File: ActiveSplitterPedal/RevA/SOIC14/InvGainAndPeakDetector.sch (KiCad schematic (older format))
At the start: 16 parts, among them U1 TL074, U5 TPS60400

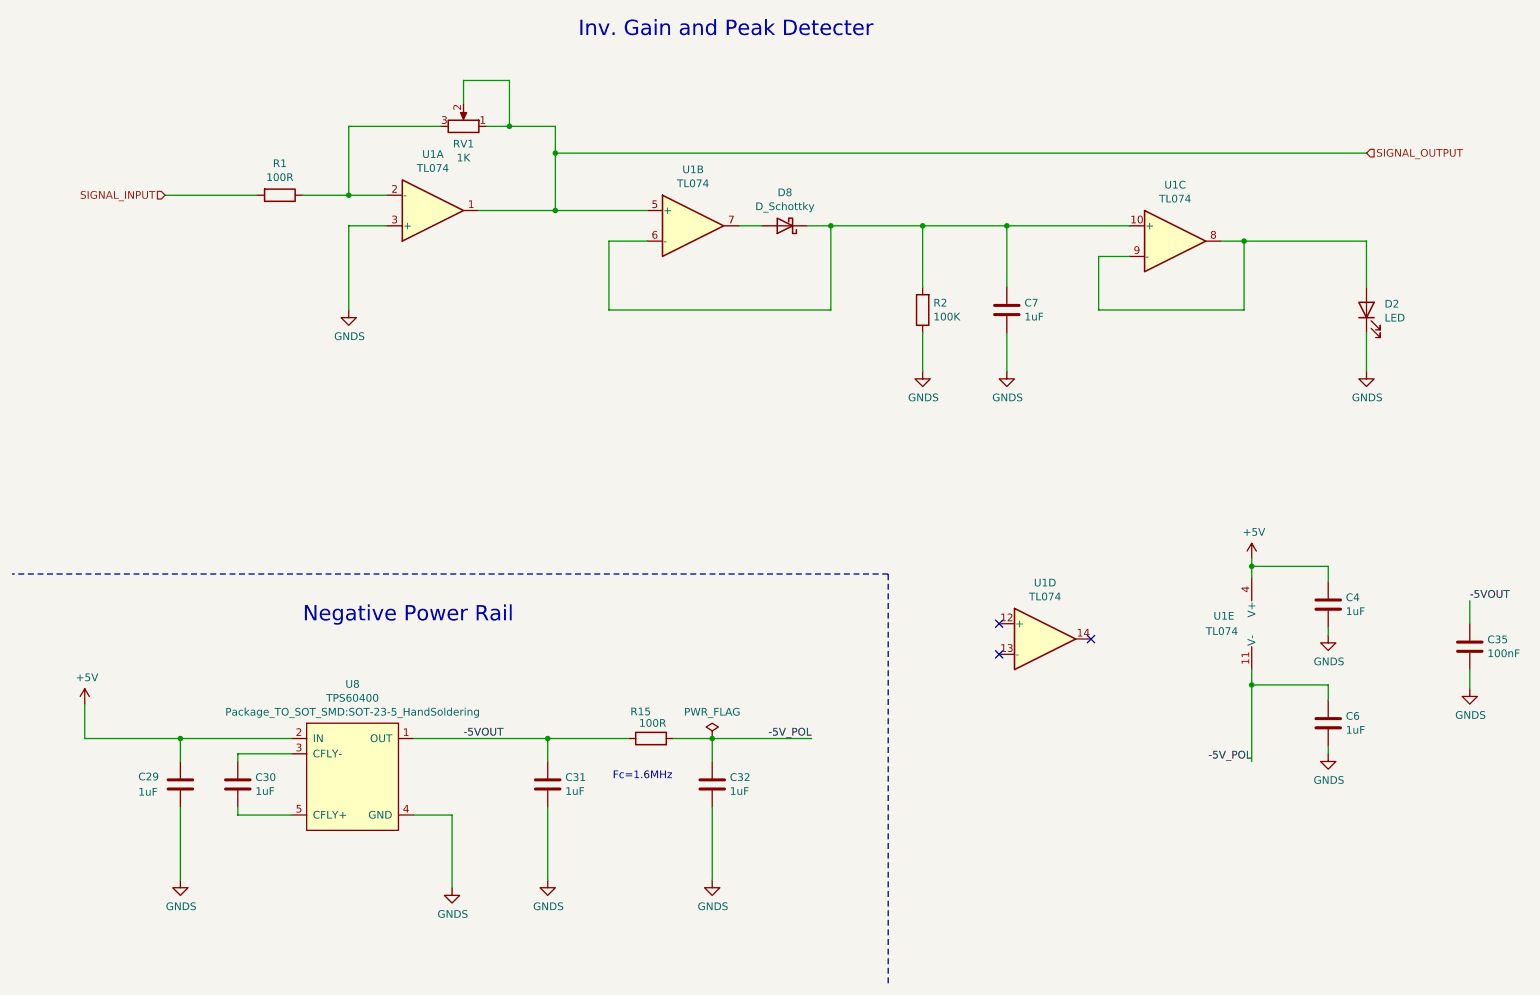
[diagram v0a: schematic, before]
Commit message: updated hw
- Updated RevA charge pump RC post  filter component values for Fc=72KHz
- Updated RevA for gain opamp components
- Branched off RevB to improve design to use internal gain for peak detector
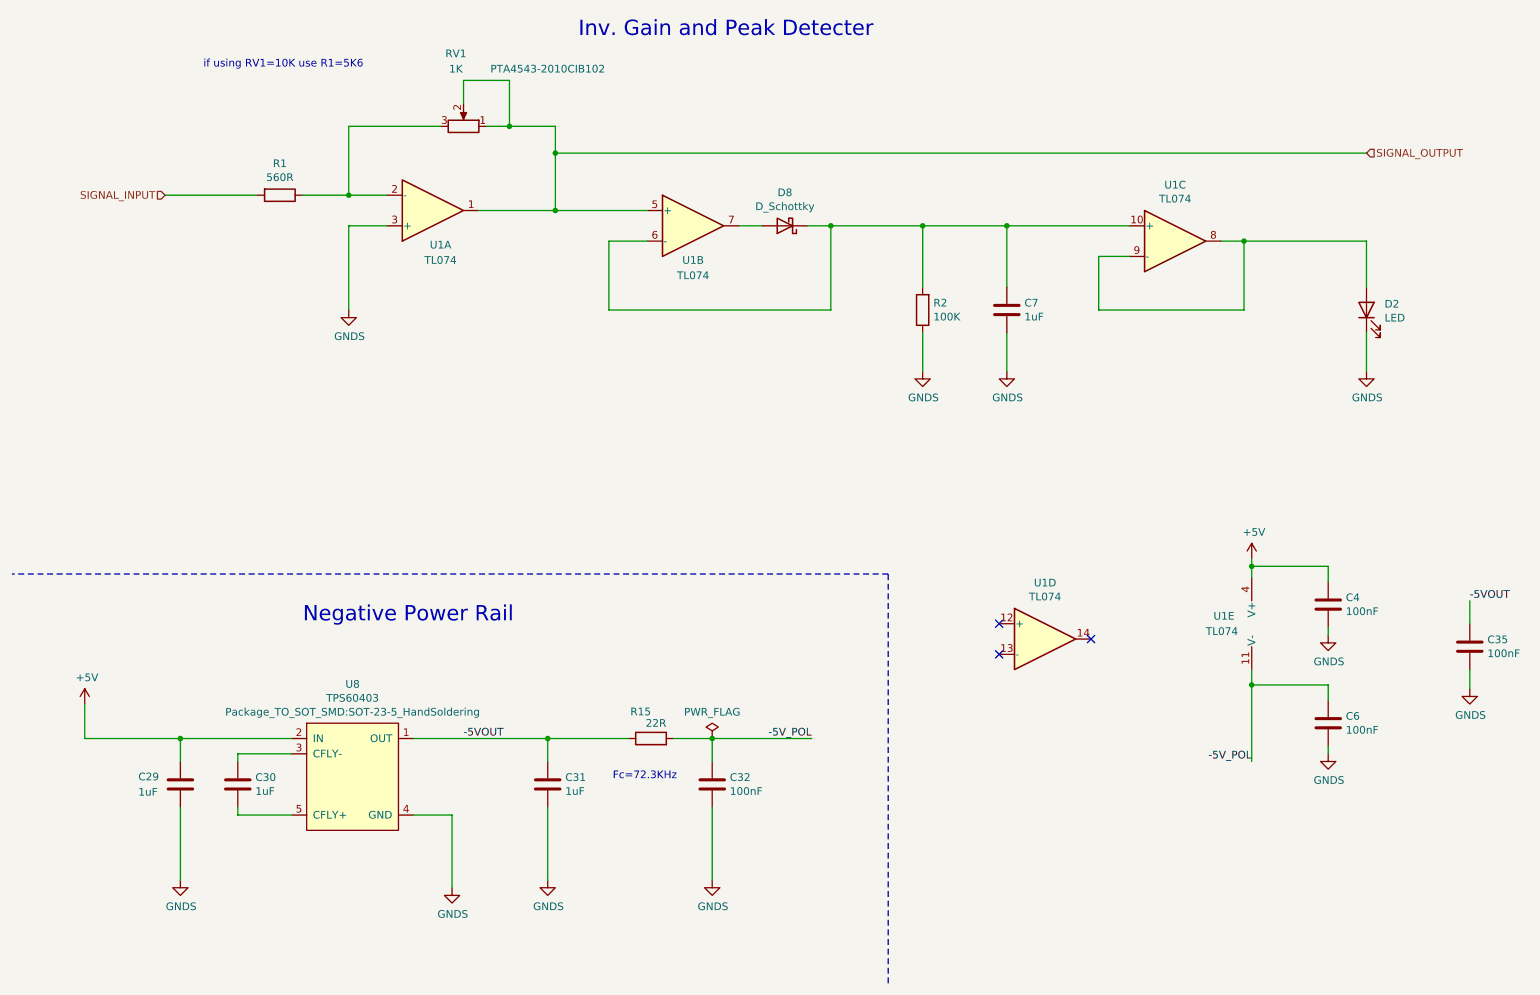
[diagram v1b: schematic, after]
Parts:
- C11, C4, C6: value 1uF -> 100nF
- R1: value 100R -> 560R
- R8: value 100R -> 22R
- RV1: Part No. (none) -> PTA4543-2010CIB102
- U5: value TPS60400 -> TPS60403
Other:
- note added: "Fc=72.3KHz"
- note added: "if using RV1=10K use R1=5K6"
- note removed: "Fc=1.6MHz"
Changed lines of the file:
@@
 $Descr A4 11693 8268
 encoding utf-8
-Sheet 6 6
+Sheet 3 6
 Title ""
 Date ""
@@
 AR Path="/5F515E89/5F3F57C8" Ref="U3"  Part="1"
 AR Path="/5F519B24/5F3F57C8" Ref="U4"  Part="1"
-F 0 "U1" H 3500 2158 50  0000 C CNN
-F 1 "TL074" H 3500 2249 50  0000 C CNN
+F 0 "U1" H 3550 2750 50  0000 C CNN
+F 1 "TL074" H 3550 2850 50  0000 C CNN
 F 2 "Package_SO:SOIC-14_3.9x8.7mm_P1.27mm" H 3450 2625 50  0001 C CNN
 F 3 "http://www.ti.com/lit/ds/symlink/tl071.pdf" H 3550 2725 50  0001 C CNN
@@
 AR Path="/5F515E89/5F3F63C2" Ref="U3"  Part="2"
 AR Path="/5F519B24/5F3F63C2" Ref="U4"  Part="2"
-F 0 "U1" H 5200 2992 50  0000 C CNN
-F 1 "TL074" H 5200 2901 50  0000 C CNN
+F 0 "U1" H 5200 2400 50  0000 C CNN
+F 1 "TL074" H 5200 2300 50  0000 C CNN
 F 2 "Package_SO:SOIC-14_3.9x8.7mm_P1.27mm" H 5150 2725 50  0001 C CNN
 F 3 "http://www.ti.com/lit/ds/symlink/tl071.pdf" H 5250 2825 50  0001 C CNN
@@
 AR Path="/5F519B24/5F415E0A" Ref="R11"  Part="1"
 F 0 "R1" V 2293 2425 50  0000 C CNN
-F 1 "100R" V 2384 2425 50  0000 C CNN
+F 1 "560R" V 2384 2425 50  0000 C CNN
 F 2 "Resistor_SMD:R_0805_2012Metric_Pad1.15x1.40mm_HandSolder" V 2430 2425 50  0001 C CNN
 F 3 "~" H 2500 2425 50  0001 C CNN
@@
 AR Path="/5F515E89/5F4179D2" Ref="RV3"  Part="1"
 AR Path="/5F519B24/5F4179D2" Ref="RV4"  Part="1"
-F 0 "RV1" V 3585 1975 50  0000 C CNN
-F 1 "1K" V 3494 1975 50  0000 C CNN
+F 0 "RV1" V 4175 1925 50  0000 C CNN
+F 1 "1K" V 4075 1925 50  0000 C CNN
 F 2 "Bourn_PTA_Slider:Slider_PTA4543_60MM" H 3700 1975 50  0001 C CNN
 F 3 "~" H 3700 1975 50  0001 C CNN
+F 4 "PTA4543-2010CIB102" V 4075 2525 50  0000 C CNN "Part No."
 	1    3700 1975
 	0    1    -1   0
@@
 AR Path="/5F519B24/5F44F4A6" Ref="C19"  Part="1"
 F 0 "C6" H 9465 5921 50  0000 L CNN
-F 1 "1uF" H 9465 5830 50  0000 L CNN
+F 1 "100nF" H 9465 5830 50  0000 L CNN
 F 2 "Capacitor_SMD:C_0805_2012Metric_Pad1.15x1.40mm_HandSolder" H 9388 5725 50  0001 C CNN
 F 3 "~" H 9350 5875 50  0001 C CNN
@@
 AR Path="/5F519B24/5F45B6FE" Ref="C18"  Part="1"
 F 0 "C4" H 9465 5146 50  0000 L CNN
-F 1 "1uF" H 9465 5055 50  0000 L CNN
+F 1 "100nF" H 9465 5055 50  0000 L CNN
 F 2 "Capacitor_SMD:C_0805_2012Metric_Pad1.15x1.40mm_HandSolder" H 9388 4950 50  0001 C CNN
 F 3 "~" H 9350 5100 50  0001 C CNN
@@
 -5VOUT
 Text Notes 4675 6250 0    50   ~ 0
-Fc=1.6MHz
+Fc=72.3KHz
 Wire Wire Line
 	5325 5975 5975 5975
@@
 AR Path="/5F3F1F31/5F414AF0" Ref="R15"  Part="1"
 F 0 "R15" V 5100 5975 50  0000 L CNN
-F 1 "100R" V 5025 5875 50  0000 L CNN
+F 1 "22R" V 5025 5875 50  0000 L CNN
 F 2 "Resistor_SMD:R_0805_2012Metric_Pad1.15x1.40mm_HandSolder" V 4855 5975 50  0001 C CNN
 F 3 "~" H 4925 5975 50  0001 C CNN
@@
 AR Path="/5F3F1F31/5F414AE2" Ref="C32"  Part="1"
 F 0 "C32" H 5440 6321 50  0000 L CNN
-F 1 "1uF" H 5440 6230 50  0000 L CNN
+F 1 "100nF" H 5440 6230 50  0000 L CNN
 F 2 "Capacitor_SMD:C_0805_2012Metric_Pad1.15x1.40mm_HandSolder" H 5363 6125 50  0001 C CNN
 F 3 "~" H 5325 6275 50  0001 C CNN
@@
 AR Path="/5F3F1F31/5F414AB4" Ref="U8"  Part="1"
 F 0 "U8" H 2975 6830 50  0000 C CNN
-F 1 "TPS60400" H 2975 6739 50  0000 C CNN
+F 1 "TPS60403" H 2975 6739 50  0000 C CNN
 F 2 "Package_TO_SOT_SMD:SOT-23-5_HandSoldering" H 2975 6648 50  0000 C CNN
 F 3 "http://www.ti.com/lit/ds/symlink/tps60402.pdf" H 2925 6375 50  0001 C CNN
@@
 Text Notes 4450 1400 0    100  ~ 0
 Inv. Gain and Peak Detecter
+Text Notes 2000 1600 0    50   ~ 0
+if using RV1=10K use R1=5K6
 $EndSCHEMATC
